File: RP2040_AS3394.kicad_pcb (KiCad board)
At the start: 4 copper layers, 52.6 x 67.6 mm, 131 parts, among them J1 Conn_01x03, J2 TYPE-C-31-M-12, J3 Conn_01x02, J4 Conn_01x08, J5 Conn_01x03, U1 RP2040, U2 NCP1117-3.3_SOT223, U3 W25Q128JVS, U4 LM324, U5 AS3394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

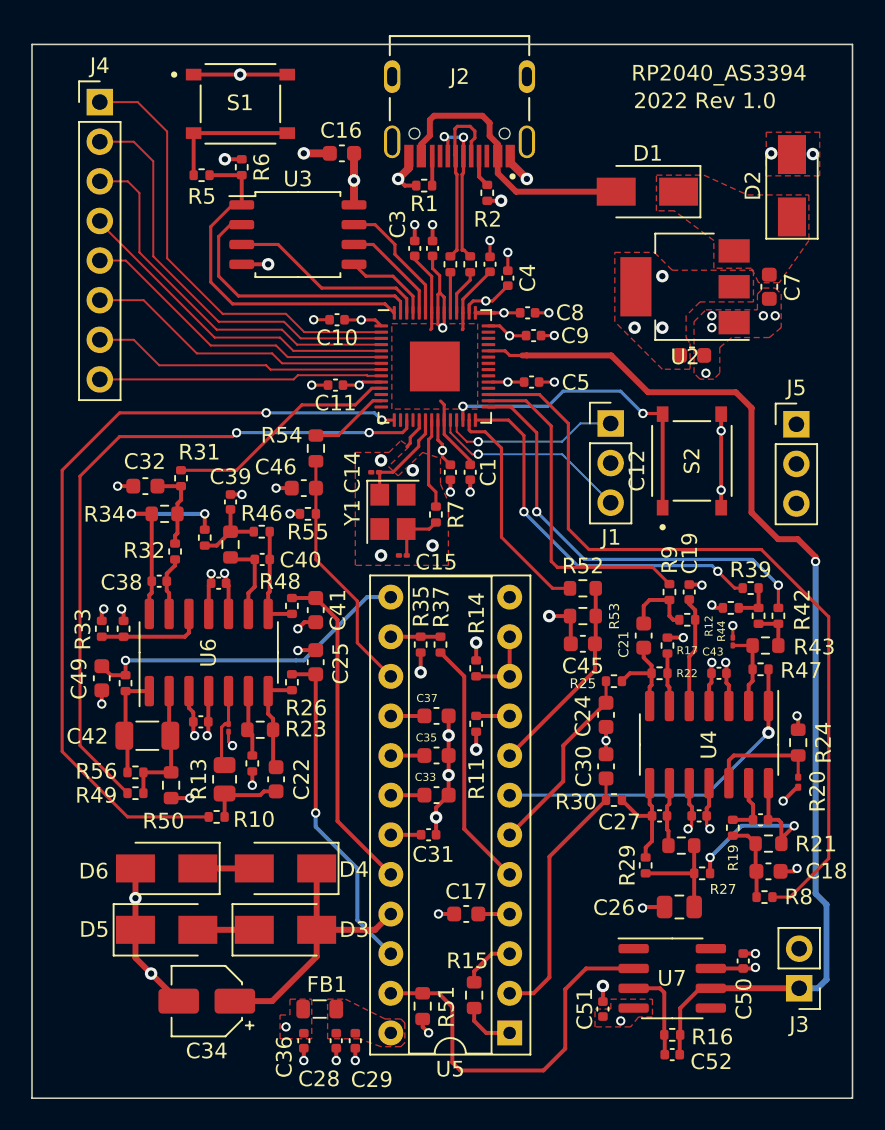
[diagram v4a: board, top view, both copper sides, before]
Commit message: First board prototype ordered from JLC with assembly
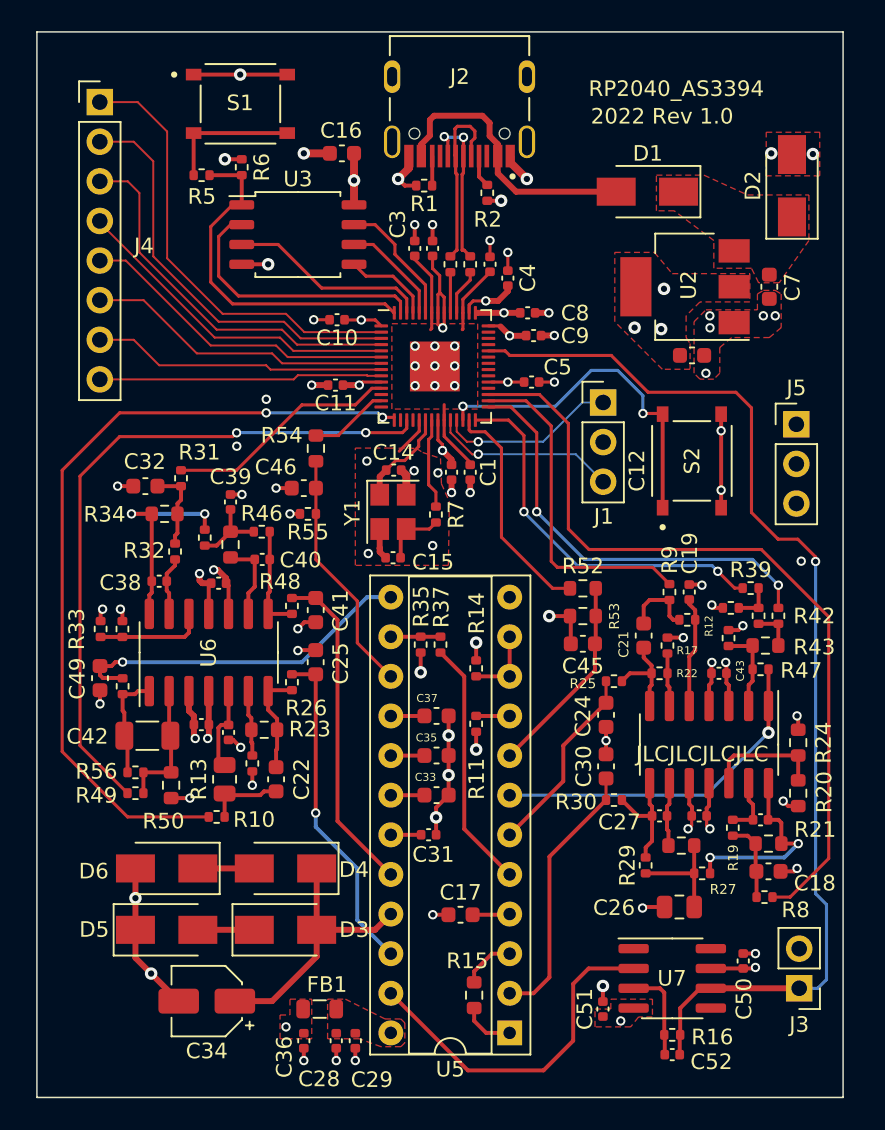
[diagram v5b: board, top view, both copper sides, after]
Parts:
- removed R51: DNF (through hole), Resistor_SMD:R_0603_1608Metric
- C14, C15, C20: footprint Capacitor_SMD:C_01005_0402Metric -> Capacitor_SMD:C_0402_1005Metric
- R20: footprint Resistor_SMD:R_0201_0603Metric -> Resistor_SMD:R_0603_1608Metric
- R44: footprint Resistor_SMD:R_01005_0402Metric -> Resistor_SMD:R_0402_1005Metric
- moved J1 1.43 mm to (145.4, 107.3)
- moved C14 1.20 mm to (132.0, 111.6), turned to 180 degrees
- moved R20 0.71 mm to (157.9, 132.3)
- moved C15 0.64 mm to (132.0, 117.2)
- moved C17 0.37 mm to (136.3, 140.1)
- moved R44 0.35 mm to (153.5, 122.4)
- moved C20 0.29 mm to (121.4, 128.4)
- moved R57 0.27 mm to (114.6, 125.5)
- moved R23 0.26 mm to (123.7, 128.3)
- moved C47 0.18 mm to (119.7, 127.9)
- moved C49 0.11 mm to (113.2, 125.0)
- moved R33 0.08 mm to (113.2, 121.8)
- moved R36 0.08 mm to (114.6, 121.8)
- moved C13 0.07 mm to (135.7, 111.8)
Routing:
- net GND: track 93.9 -> 97.2 mm, vias 65 -> 77
- net /AS3394_PWM/Out: track 24.6 -> 22.5 mm
- net /RUN: track 20.9 -> 22.5 mm
- net /AS3394_PWM/Mixer_Balance_CV: track 21.4 -> 22.6 mm
- net Net-(J1-Pad3): track 12.9 -> 11.9 mm
- net VEE: track 52.3 -> 51.4 mm
- net Net-(C23-Pad2): track 13.4 -> 12.7 mm
- net Net-(C15-Pad2): track 3.79 -> 3.24 mm
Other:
- board size 52.6 x 67.6 mm -> 51.7 x 68.3 mm
- board text added: "JLCJLCJLCJLC"

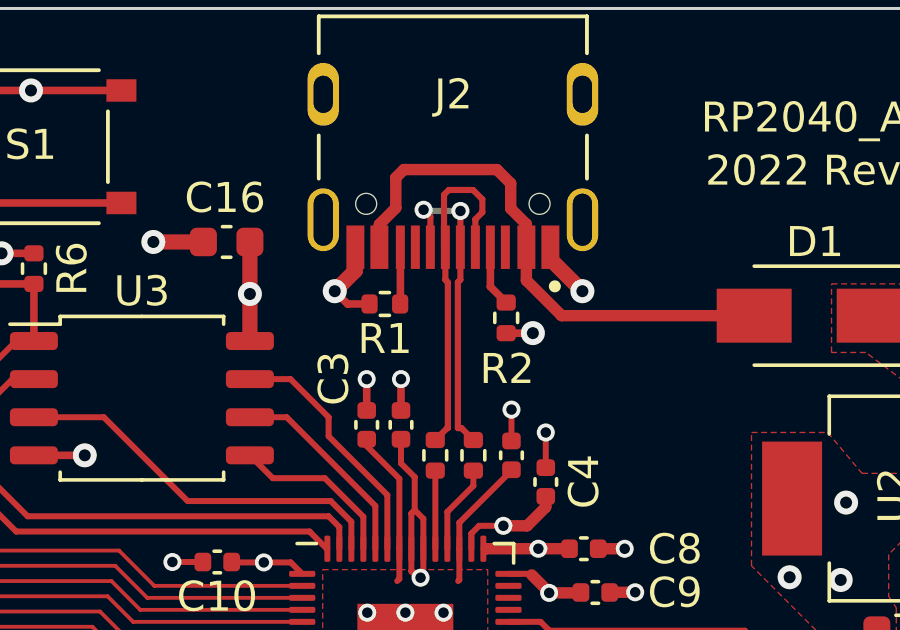
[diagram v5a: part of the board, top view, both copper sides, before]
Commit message: Fixed diff pair polarity
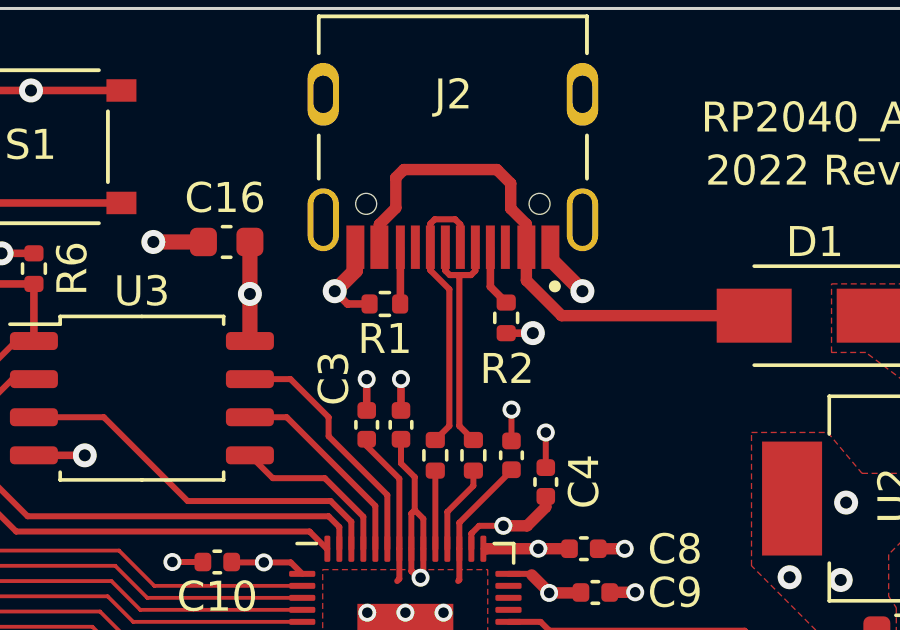
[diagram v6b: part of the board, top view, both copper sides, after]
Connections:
- J2 pad A6: /USB_D- -> /USB_D+
- J2 pad A7: /USB_D+ -> /USB_D-
- J2 pad B6: /USB_D- -> /USB_D+
- J2 pad B7: /USB_D+ -> /USB_D-
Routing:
- net /USB_D-: track 10.5 -> 8.45 mm, vias 2 -> 0
- net /USB_D+: track 11.6 -> 9.56 mm
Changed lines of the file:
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@@
     (property "Sheetfile" "RP2040_AS3394.kicad_sch")
     (property "Sheetname" "")
-    (attr smd exclude_from_pos_files exclude_from_bom)
+    (attr smd exclude_from_pos_files)
     (fp_text reference "R6" (at -0.002 -1.283 90) (layer "F.SilkS")
       (effects (font (size 1 1) (thickness 0.15)))
@@
       (net 50 "Net-(J2-PadA5)") (pinfunction "CC1") (pintype "bidirectional"))
     (pad "A6" smd rect locked (at -0.25 -5.095 180) (size 0.3 1.45) (layers "F.Cu" "F.Paste" "F.Mask")
-      (net 48 "/USB_D-") (pinfunction "DP1") (pintype "bidirectional"))
+      (net 49 "/USB_D+") (pinfunction "DP1") (pintype "bidirectional"))
     (pad "A7" smd rect locked (at 0.25 -5.095 180) (size 0.3 1.45) (layers "F.Cu" "F.Paste" "F.Mask")
-      (net 49 "/USB_D+") (pinfunction "DN1") (pintype "bidirectional"))
+      (net 48 "/USB_D-") (pinfunction "DN1") (pintype "bidirectional"))
     (pad "A8" smd rect locked (at 1.25 -5.095 180) (size 0.3 1.45) (layers "F.Cu" "F.Paste" "F.Mask")
       (net 52 "unconnected-(J2-PadA8)") (pinfunction "SBU1") (pintype "bidirectional+no_connect"))
@@
       (net 53 "Net-(J2-PadB5)") (pinfunction "CC2") (pintype "bidirectional"))
     (pad "B6" smd rect locked (at 0.75 -5.095 180) (size 0.3 1.45) (layers "F.Cu" "F.Paste" "F.Mask")
-      (net 48 "/USB_D-") (pinfunction "DP2") (pintype "bidirectional"))
+      (net 49 "/USB_D+") (pinfunction "DP2") (pintype "bidirectional"))
     (pad "B7" smd rect locked (at -0.75 -5.095 180) (size 0.3 1.45) (layers "F.Cu" "F.Paste" "F.Mask")
-      (net 49 "/USB_D+") (pinfunction "DN2") (pintype "bidirectional"))
+      (net 48 "/USB_D-") (pinfunction "DN2") (pintype "bidirectional"))
     (pad "B8" smd rect locked (at -1.75 -5.095 180) (size 0.3 1.45) (layers "F.Cu" "F.Paste" "F.Mask")
       (net 51 "unconnected-(J2-PadB8)") (pinfunction "SBU2") (pintype "bidirectional+no_connect"))
@@
     (property "Sheetfile" "RP2040_AS3394.kicad_sch")
     (property "Sheetname" "")
-    (attr through_hole exclude_from_pos_files exclude_from_bom)
+    (attr through_hole exclude_from_pos_files)
     (fp_text reference "J4" (at 2.833 9.224) (layer "F.SilkS")
       (effects (font (size 1 1) (thickness 0.15)))
@@
     (property "Sheetfile" "AS3394_PWM.kicad_sch")
     (property "Sheetname" "AS3394_PWM")
-    (attr through_hole exclude_from_pos_files exclude_from_bom)
+    (attr through_hole exclude_from_pos_files)
     (fp_text reference "U5" (at 3.81 -2.33) (layer "F.SilkS")
       (effects (font (size 1 1) (thickness 0.15)))
@@
     (property "Sheetfile" "RP2040_AS3394.kicad_sch")
     (property "Sheetname" "")
-    (attr through_hole exclude_from_pos_files exclude_from_bom)
+    (attr through_hole exclude_from_pos_files)
     (fp_text reference "J1" (at 0.04 7.31) (layer "F.SilkS")
       (effects (font (size 1 1) (thickness 0.15)))
@@
     (property "Sheetfile" "RP2040_AS3394.kicad_sch")
     (property "Sheetname" "")
-    (attr through_hole exclude_from_pos_files exclude_from_bom)
+    (attr through_hole exclude_from_pos_files)
     (fp_text reference "J3" (at 0 -2.33) (layer "F.SilkS")
       (effects (font (size 1 1) (thickness 0.15)))
@@
     (property "Sheetfile" "RP2040_AS3394.kicad_sch")
     (property "Sheetname" "")
-    (attr through_hole exclude_from_pos_files exclude_from_bom)
+    (attr through_hole exclude_from_pos_files)
     (fp_text reference "J5" (at 0 -2.33) (layer "F.SilkS")
       (effects (font (size 1 1) (thickness 0.15)))
@@
   (segment (start 137.423111 110.602902) (end 143.667902 110.602902) (width 0.127) (layer "B.Cu") (net 47))
   (segment (start 143.667902 110.602902) (end 145.43 112.365) (width 0.127) (layer "B.Cu") (net 47))
-  (segment (start 136.38837 92.658631) (end 136.38837 97.51866) (width 0.20574) (layer "F.Cu") (net 48))
-  (segment (start 136.50966 97.51866) (end 136.906 97.915) (width 0.20574) (layer "F.Cu") (net 48))
-  (segment (start 136.38837 97.51866) (end 136.50966 97.51866) (width 0.20574) (layer "F.Cu") (net 48))
-  (segment (start 136.472 91.4875) (end 136.472 90.283) (width 0.20574) (layer "F.Cu") (net 48))
-  (segment (start 136.472 92.575001) (end 136.38837 92.658631) (width 0.20574) (layer "F.Cu") (net 48))
-  (segment (start 135.472 90.467) (end 135.472 91.4875) (width 0.20574) (layer "F.Cu") (net 48))
-  (segment (start 136.472 90.283) (end 136.475 90.28) (width 0.20574) (layer "F.Cu") (net 48))
-  (segment (start 135.245 90.24) (end 135.472 90.467) (width 0.20574) (layer "F.Cu") (net 48))
-  (segment (start 136.472 91.4875) (end 136.472 92.575001) (width 0.20574) (layer "F.Cu") (net 48))
-  (via (at 136.475 90.28) (size 0.6) (drill 0.35) (layers "F.Cu" "B.Cu") (net 48))
-  (via (at 135.245 90.24) (size 0.6) (drill 0.35) (layers "F.Cu" "B.Cu") (net 48))
-  (segment (start 135.285 90.28) (end 135.245 90.24) (width 0.20574) (layer "B.Cu") (net 48))
-  (segment (start 136.475 90.28) (end 135.285 90.28) (width 0.20574) (layer "B.Cu") (net 48))
-  (segment (start 136.085 89.58) (end 135.92713 89.73787) (width 0.20574) (layer "F.Cu") (net 49))
-  (segment (start 137.205 89.89) (end 136.895 89.58) (width 0.20574) (layer "F.Cu") (net 49))
-  (segment (start 135.92713 91.44263) (end 135.972 91.4875) (width 0.20574) (layer "F.Cu") (net 49))
-  (segment (start 137.205 90.32376) (end 137.205 89.89) (width 0.20574) (layer "F.Cu") (net 49))
-  (segment (start 135.972 92.575001) (end 136.05563 92.658631) (width 0.20574) (layer "F.Cu") (net 49))
-  (segment (start 135.92713 89.73787) (end 135.92713 91.44263) (width 0.20574) (layer "F.Cu") (net 49))
-  (segment (start 136.05563 97.51866) (end 136.03234 97.51866) (width 0.20574) (layer "F.Cu") (net 49))
-  (segment (start 136.895 89.58) (end 136.085 89.58) (width 0.20574) (layer "F.Cu") (net 49))
-  (segment (start 136.05563 92.658631) (end 136.05563 97.51866) (width 0.20574) (layer "F.Cu") (net 49))
-  (segment (start 135.972 91.4875) (end 135.972 92.575001) (width 0.20574) (layer "F.Cu") (net 49))
-  (segment (start 136.972 90.55676) (end 137.205 90.32376) (width 0.20574) (layer "F.Cu") (net 49))
-  (segment (start 136.03234 97.51866) (end 135.636 97.915) (width 0.20574) (layer "F.Cu") (net 49))
-  (segment (start 136.972 91.4875) (end 136.972 90.55676) (width 0.20574) (layer "F.Cu") (net 49))
+  (segment (start 136.42303 92.41697) (end 136.82647 92.41697) (width 0.20574) (layer "F.Cu") (net 48))
+  (segment (start 136.11753 92.41697) (end 136.42303 92.41697) (width 0.20574) (layer "F.Cu") (net 48))
+  (segment (start 136.82647 92.41697) (end 136.972 92.27144) (width 0.20574) (layer "F.Cu") (net 48))
+  (segment (start 135.972 91.4875) (end 135.972 92.27144) (width 0.20574) (layer "F.Cu") (net 48))
+  (segment (start 136.906 97.915) (end 136.43737 97.44637) (width 0.20574) (layer "F.Cu") (net 48))
+  (segment (start 135.92713 91.44263) (end 135.972 91.4875) (width 0.20574) (layer "F.Cu") (net 48))
+  (segment (start 136.972 92.27144) (end 136.972 91.4875) (width 0.20574) (layer "F.Cu") (net 48))
+  (segment (start 136.43737 97.44637) (end 136.43737 92.43131) (width 0.20574) (layer "F.Cu") (net 48))
+  (segment (start 135.972 92.27144) (end 136.11753 92.41697) (width 0.20574) (layer "F.Cu") (net 48))
+  (segment (start 136.43737 92.43131) (end 136.42303 92.41697) (width 0.20574) (layer "F.Cu") (net 48))
+  (segment (start 136.472 90.732) (end 136.472 91.4875) (width 0.20574) (layer "F.Cu") (net 49))
+  (segment (start 135.472 91.4875) (end 135.472 90.70356) (width 0.20574) (layer "F.Cu") (net 49))
+  (segment (start 135.472 92.25755) (end 135.472 91.4875) (width 0.20574) (layer "F.Cu") (net 49))
+  (segment (start 136.10463 97.44637) (end 136.10463 92.89018) (width 0.20574) (layer "F.Cu") (net 49))
+  (segment (start 136.29803 90.55803) (end 136.472 90.732) (width 0.20574) (layer "F.Cu") (net 49))
+  (segment (start 135.61753 90.55803) (end 136.29803 90.55803) (width 0.20574) (layer "F.Cu") (net 49))
+  (segment (start 135.636 97.915) (end 136.10463 97.44637) (width 0.20574) (layer "F.Cu") (net 49))
+  (segment (start 135.472 90.70356) (end 135.61753 90.55803) (width 0.20574) (layer "F.Cu") (net 49))
+  (segment (start 136.10463 92.89018) (end 135.472 92.25755) (width 0.20574) (layer "F.Cu") (net 49))
   (segment (start 137.472 91.4875) (end 137.472 92.805) (width 0.254) (layer "F.Cu") (net 50))
   (segment (start 137.472 92.805) (end 138 93.333) (width 0.254) (layer "F.Cu") (net 50))

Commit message: continuing work on second version
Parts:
- D3, D4, D5, D6: footprint Diode_SMD:D_SMA -> Diode_SMD:D_SOD-123
- moved J5 55.8 mm to (111.5, 139.7)
- moved C34 9.07 mm to (116.0, 137.6), turned to 90 degrees
- moved D5 4.40 mm to (121.0, 138.6)
- moved D6 3.85 mm to (121.0, 135.8)
- moved D3 2.80 mm to (126.2, 138.6)
- moved C17 2.08 mm to (137.3, 138.3), turned to -90 degrees
- moved D4 1.83 mm to (126.2, 135.8)
- moved J4 1.69 mm to (111.5, 88.0)
- moved C51 0.14 mm to (145.4, 146.3)
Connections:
- C52 pad 1: Net-(C52-Pad1) -> /AS3394_PWM/Out
- R16 pad 1: Net-(C52-Pad1) -> /AS3394_PWM/Out
- U7 pad 3: Net-(C52-Pad1) -> GND
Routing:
- net /AS3394_PWM/Out: track 22.5 -> 29.7 mm
- net Net-(C52-Pad1): track 6.07 -> 0.00 mm
- net Net-(C34-Pad1): track 17.3 -> 20.7 mm
- net Net-(J4-Pad4): track 21.6 -> 24.4 mm
- net Net-(D4-Pad2): track 3.62 -> 1.91 mm
- net Net-(D3-Pad1): track 3.62 -> 1.91 mm
- net Net-(J4-Pad5): track 20.6 -> 22.3 mm
- net Net-(J4-Pad8): track 18.2 -> 19.9 mm
- net Net-(J4-Pad7): track 18.8 -> 20.5 mm
- net Net-(J4-Pad6): track 19.7 -> 21.4 mm
- net GND: track 97.2 -> 95.9 mm
- net Net-(J4-Pad3): track 24.6 -> 25.9 mm
- net /AMP_OUT: track 70.9 -> 70.2 mm
- net Net-(C17-Pad2): track 2.34 -> 2.93 mm
- net Net-(J4-Pad2): track 26.8 -> 27.4 mm
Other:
- board size 51.7 x 68.3 mm -> 51.8 x 68.3 mm
- board text added: "0"
- board text added: "1"
- board text added: "2"
- board text added: "2022 Rev 1.1"
- board text added: "3"
- board text added: "4"
- board text added: "5"
- board text added: "6"
- board text added: "7"
- board text added: "GPIO"
- board text removed: "2022 Rev 1.0"
